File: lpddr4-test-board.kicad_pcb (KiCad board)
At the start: 8 copper layers, 117 x 86 mm, 266 parts, among them IC1 TPS54561, IC3 TPD8S009DSMR, J1 0878311420, J10 61300311121, J2 08B0-1X1T-36-F, J3 DC_SOCKET, J4 WE_629105150521, J5 2309409-1, J6 685119134923, J7 1140084168, Q2 BSS138APW, Q3 BSS138APW, Q4 BSS138APW, Q5 BSS138APW, Q6 BSS138APW, Q7 BSS138APW, Q8 BSS138APW, U1 XC7K70T-FBG484, U2 ASEM1-100.000MHZ-LC-T, U3 S25FL128SAGNFI000, U4 TPS65296, U5 TPS62823DLCT, U6 DP83848JSQ_NOPB, U7 FT4232HQ, Y1 ABM8G-25.000MHZ-18-D2Y-T

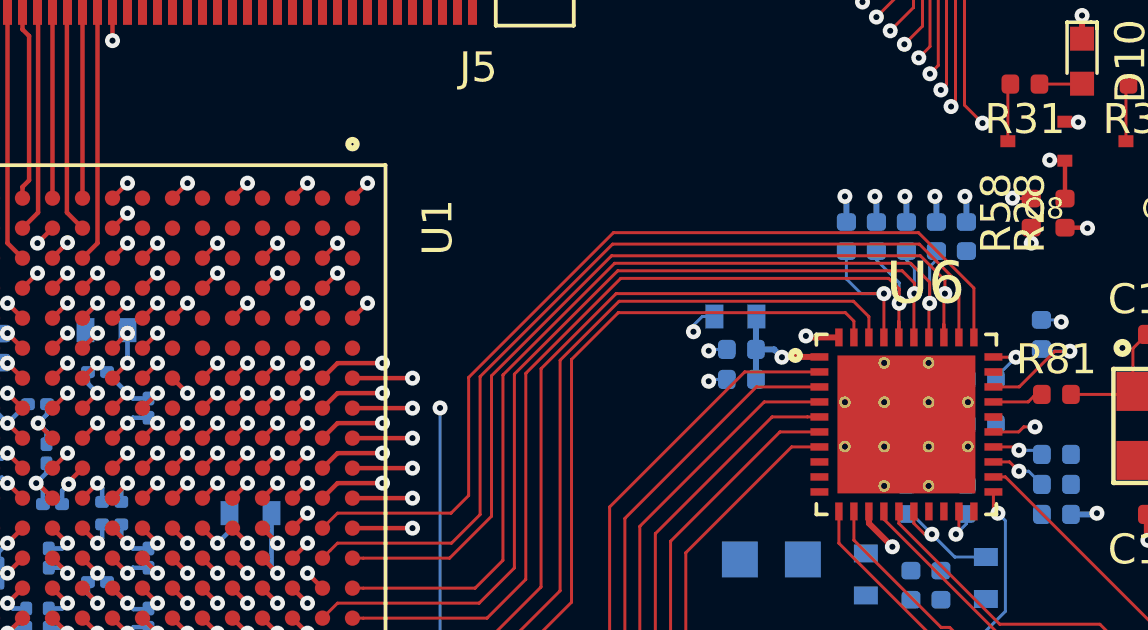
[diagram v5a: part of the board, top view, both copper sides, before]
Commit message: Change via assignment under FPGA
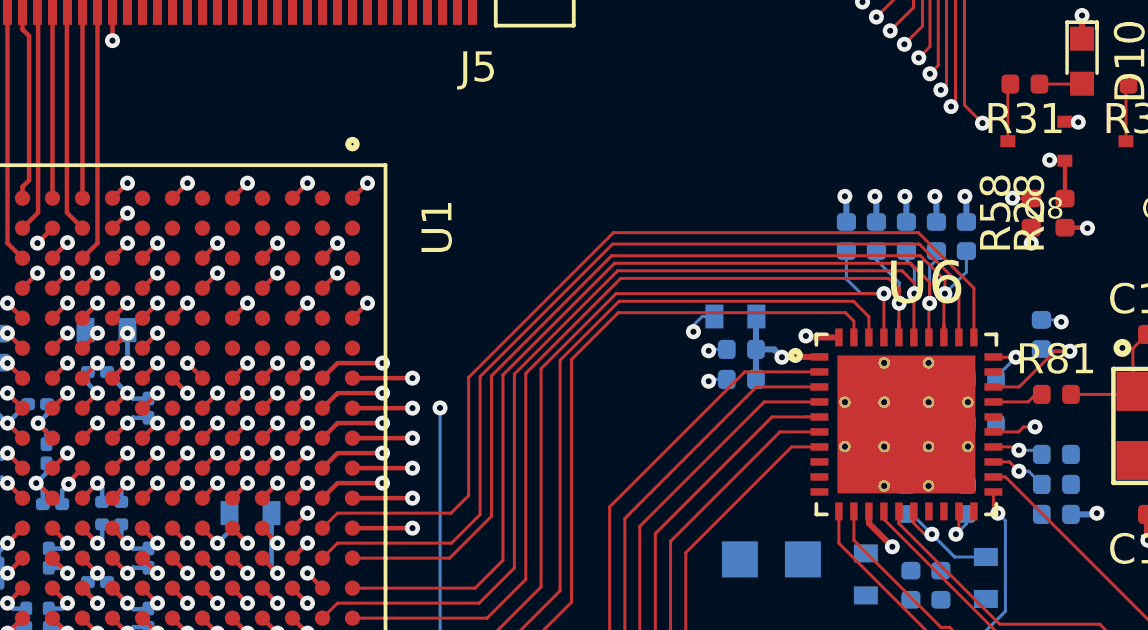
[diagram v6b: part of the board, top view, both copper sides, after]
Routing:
- net ETH_CRS: track 29.4 -> 31.1 mm
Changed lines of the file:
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@@
     (thickness 1.6)
     (drawings 130)
-    (tracks 3293)
+    (tracks 3297)
     (zones 0)
     (modules 266)
@@
   (segment (start 173.536329 89.497157) (end 174.036329 88.997157) (width 0.15) (layer F.Cu) (net 19))
   (via blind (at 174.036329 88.997157) (size 0.5) (drill 0.2) (layers F.Cu GND1) (net 19) (status 40000))
-  (segment (start 174.536329 91.497157) (end 175.036329 90.997156) (width 0.15) (layer F.Cu) (net 19))
-  (via blind (at 175.036329 90.997156) (size 0.5) (drill 0.2) (layers F.Cu GND1) (net 19) (status 40000))
+  (segment (start 174.536328 91.497156) (end 174.036327 90.997156) (width 0.15) (layer F.Cu) (net 19))
+  (via (at 174.036327 90.997156) (size 0.5) (drill 0.2) (layers F.Cu B.Cu) (net 19) (status 40000))
   (segment (start 175.536329 94.497156) (end 176.036328 93.997157) (width 0.15) (layer F.Cu) (net 19))
   (segment (start 175.536328 89.497157) (end 176.036328 88.997157) (width 0.15) (layer F.Cu) (net 19))
@@
   (segment (start 206.278 71.773) (end 204.506 71.773) (width 0.15) (layer F.Cu) (net 23))
   (segment (start 204.506 71.773) (end 204.49 71.789) (width 0.15) (layer F.Cu) (net 23))
-  (segment (start 204.49 75.726) (end 204.49 71.789) (width 0.1) (layer In2.Cu) (net 23))
-  (segment (start 196.1715 77.6945) (end 202.5215 77.6945) (width 0.1) (layer In2.Cu) (net 23))
-  (segment (start 171.370327 90.997156) (end 171.847171 91.474) (width 0.1) (layer In2.Cu) (net 23))
-  (segment (start 173.248 91.474) (end 174.264 90.458) (width 0.1) (layer In2.Cu) (net 23))
-  (segment (start 171.036329 90.997156) (end 171.370327 90.997156) (width 0.1) (layer In2.Cu) (net 23))
-  (segment (start 171.847171 91.474) (end 173.248 91.474) (width 0.1) (layer In2.Cu) (net 23))
-  (segment (start 174.264 90.458) (end 183.408 90.458) (width 0.1) (layer In2.Cu) (net 23))
-  (segment (start 202.5215 77.6945) (end 204.49 75.726) (width 0.1) (layer In2.Cu) (net 23))
-  (segment (start 183.408 90.458) (end 196.1715 77.6945) (width 0.1) (layer In2.Cu) (net 23))
   (segment (start 170.411328 90.997157) (end 171.036329 90.997156) (width 0.1) (layer In5.Cu) (net 23))
   (segment (start 168.620327 89.247157) (end 170.370327 90.997157) (width 0.1) (layer In5.Cu) (net 23))
@@
   (segment (start 153.161328 104.997157) (end 152.036328 106.122157) (width 0.1) (layer In5.Cu) (net 23))
   (segment (start 157.286328 89.247157) (end 157.536328 89.247157) (width 0.1) (layer In5.Cu) (net 23))
+  (segment (start 202.5215 77.6945) (end 204.49 75.726) (width 0.1) (layer In2.Cu) (net 23))
+  (segment (start 176.450485 90.458) (end 183.408 90.458) (width 0.1) (layer In2.Cu) (net 23))
+  (segment (start 175.434485 91.474) (end 176.450485 90.458) (width 0.1) (layer In2.Cu) (net 23))
+  (segment (start 196.1715 77.6945) (end 202.5215 77.6945) (width 0.1) (layer In2.Cu) (net 23))
+  (segment (start 171.370327 90.997156) (end 171.847171 91.474) (width 0.1) (layer In2.Cu) (net 23))
+  (segment (start 171.036329 90.997156) (end 171.370327 90.997156) (width 0.1) (layer In2.Cu) (net 23))
+  (segment (start 204.49 75.726) (end 204.49 71.789) (width 0.1) (layer In2.Cu) (net 23))
+  (segment (start 171.847171 91.474) (end 175.434485 91.474) (width 0.1) (layer In2.Cu) (net 23))
+  (segment (start 183.408 90.458) (end 196.1715 77.6945) (width 0.1) (layer In2.Cu) (net 23))
   (segment (start 169.536329 90.497157) (end 170.036329 89.997157) (width 0.15) (layer F.Cu) (net 24))
   (via blind (at 170.036329 89.997157) (size 0.5) (drill 0.2) (layers F.Cu In5.Cu) (net 24) (status 40000))
@@
   (segment (start 184.17 91.419136) (end 184.17 96.100866) (width 0.1) (layer F.Cu) (net 41))
   (segment (start 199.283 88.235502) (end 198.465478 87.41798) (width 0.1) (layer F.Cu) (net 41))
+  (segment (start 200 87.963) (end 199.283 88.68) (width 0.1) (layer B.Cu) (net 41))
+  (segment (start 200 87.263) (end 200 87.963) (width 0.1) (layer B.Cu) (net 41))
   (via (at 198.267 88.68) (size 0.5) (drill 0.2) (layers F.Cu B.Cu) (net 42))
   (segment (start 198.25 88.697) (end 198.267 88.68) (width 0.1) (layer F.Cu) (net 42))
@@
   (via blind (at 175.036329 91.997157) (size 0.5) (drill 0.2) (layers F.Cu In2.Cu) (net 90) (status 40000))
   (via (at 196.536328 78.95899) (size 0.5) (drill 0.2) (layers F.Cu B.Cu) (net 90))
-  (segment (start 196.109755 78.95899) (end 196.536328 78.95899) (width 0.1) (layer In2.Cu) (net 90))
-  (segment (start 184.181588 90.887157) (end 196.109755 78.95899) (width 0.1) (layer In2.Cu) (net 90))
-  (segment (start 176.146329 90.887157) (end 184.181588 90.887157) (width 0.1) (layer In2.Cu) (net 90))
-  (segment (start 175.036329 91.997157) (end 176.146329 90.887157) (width 0.1) (layer In2.Cu) (net 90))
   (segment (start 197.736328 77.75899) (end 196.536328 78.95899) (width 0.1) (layer F.Cu) (net 90))
   (segment (start 197.736328 73.397157) (end 197.736328 77.75899) (width 0.1) (layer F.Cu) (net 90))
@@
   (segment (start 190.036328 96.247157) (end 180.036328 96.247157) (width 0.1) (layer In2.Cu) (net 57))
   (segment (start 201.536328 93.122157) (end 201.286328 92.872157) (width 0.1) (layer In2.Cu) (net 57))
+  (segment (start 175.036329 91.997157) (end 175.389882 91.997157) (width 0.1) (layer In2.Cu) (net 90))
+  (segment (start 196.182775 78.95899) (end 196.536328 78.95899) (width 0.1) (layer In2.Cu) (net 90))
+  (segment (start 196.109755 78.95899) (end 196.182775 78.95899) (width 0.1) (layer In2.Cu) (net 90))
+  (segment (start 176.499882 90.887157) (end 184.181588 90.887157) (width 0.1) (layer In2.Cu) (net 90))
+  (segment (start 184.181588 90.887157) (end 196.109755 78.95899) (width 0.1) (layer In2.Cu) (net 90))
+  (segment (start 175.389882 91.997157) (end 176.499882 90.887157) (width 0.1) (layer In2.Cu) (net 90))
   (via (at 175.036329 99.997156) (size 0.5) (drill 0.2) (layers F.Cu B.Cu) (net 129) (status 40000))
   (segment (start 174.536329 99.497156) (end 175.036329 99.997156) (width 0.15) (layer F.Cu) (net 129))

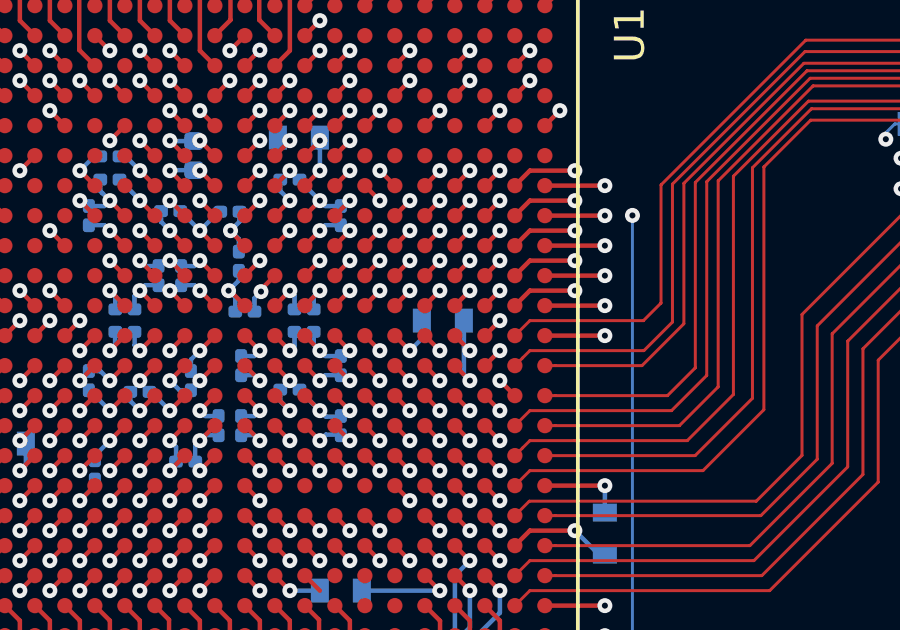
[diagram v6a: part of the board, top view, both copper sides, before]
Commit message: Change RGMII control signal assignment
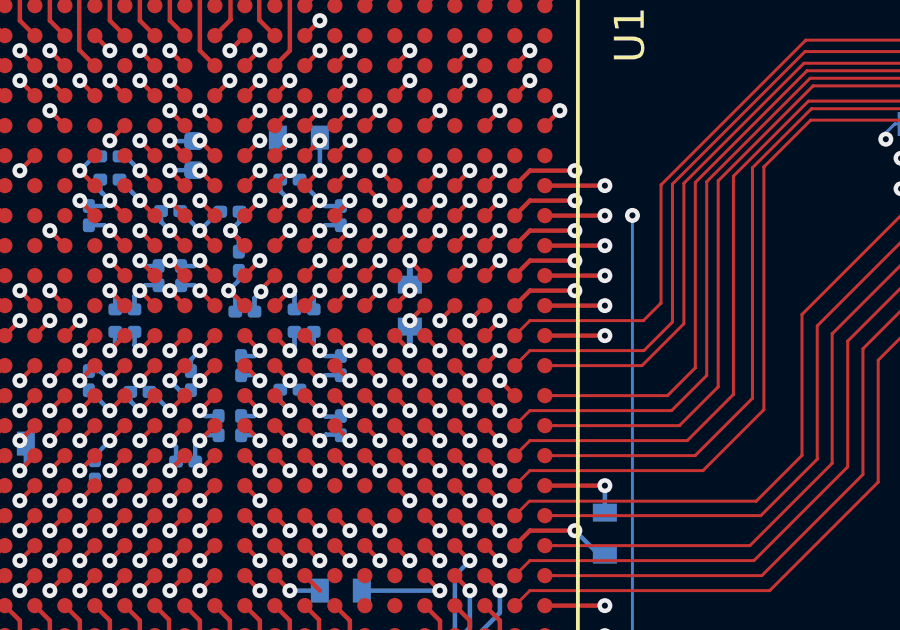
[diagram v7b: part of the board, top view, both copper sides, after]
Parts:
- moved C3 1.21 mm to (175.0, 95.5), turned to 90 degrees
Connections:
- U1 pad C12: ETH_MDIO -> ETH_REF_CLK
- U1 pad C13: ETH_TX_RSTN -> ETH_MDIO
- U1 pad C15: ETH_REF_CLK -> Net-(U1-PadC15)
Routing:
- net ETH_MDC: track 25.9 -> 31.0 mm
- net ETH_MDIO: track 26.5 -> 28.1 mm
- net ETH_TX_RSTN: track 1.46 -> 0.00 mm, vias 1 -> 0
- net GND: track 212.3 -> 211.3 mm
- net ETH_REF_CLK: track 28.4 -> 29.4 mm
- net Net-(U1-PadF10): track 0.71 -> 0.00 mm, vias 1 -> 0
- net Net-(U1-PadC15): track 0.00 -> 0.71 mm, vias 0 -> 1

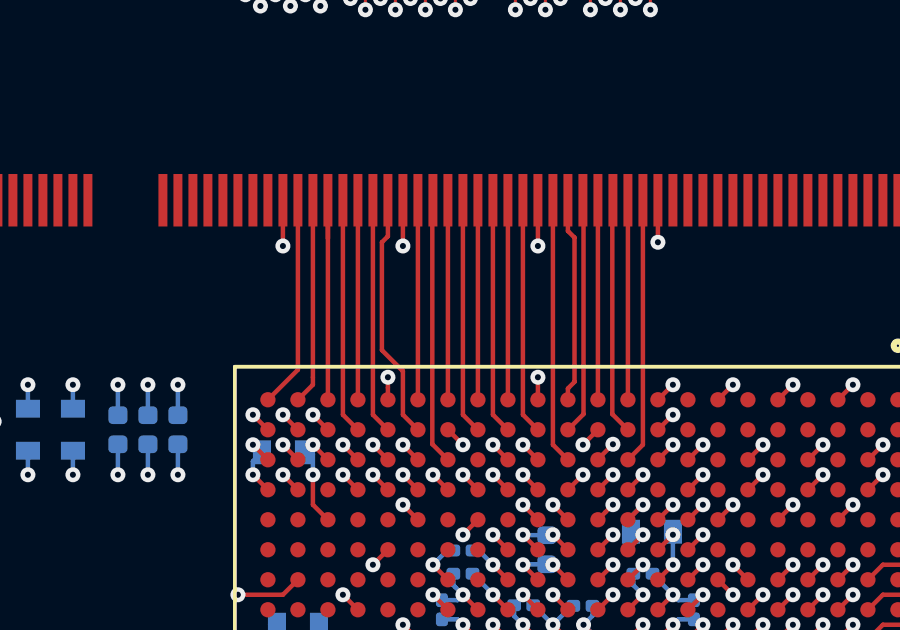
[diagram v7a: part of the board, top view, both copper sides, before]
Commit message: Update RGMII connector, started DRAM DQ equalization
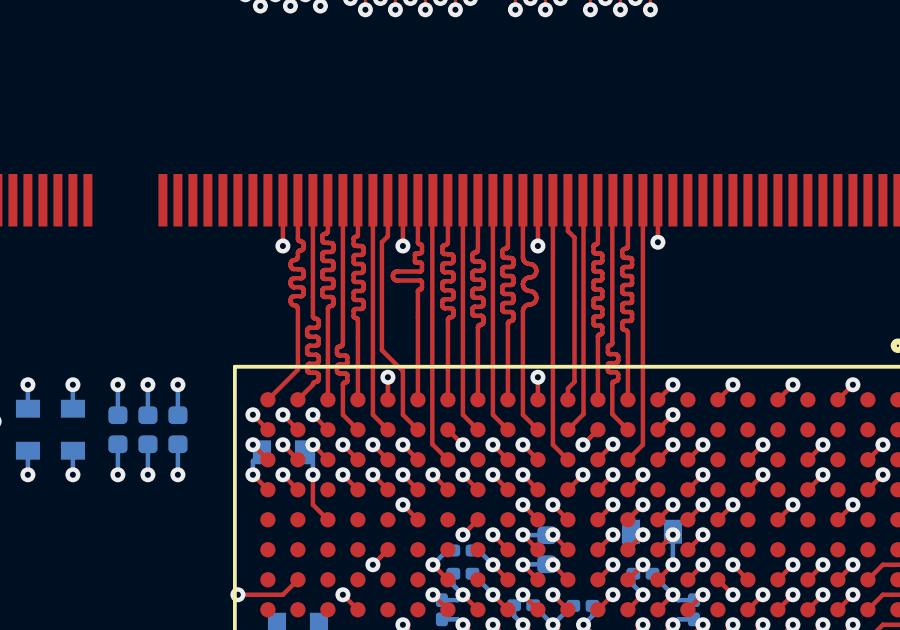
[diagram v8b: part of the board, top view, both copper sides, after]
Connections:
- U1 pad C15: Net-(U1-PadC15) -> ETH_RSTN
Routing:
- net ETH_RSTN: track 1.93 -> 30.7 mm, vias 1 -> 2
- net Net-(J5-Pad192): track 0.00 -> 19.2 mm, vias 0 -> 2
- net IO_N5: track 19.2 -> 0.00 mm, vias 2 -> 0
- net DMI_1A: track 6.62 -> 8.91 mm
- net DQ15_A: track 6.65 -> 8.93 mm
- net DQ04_A: track 6.65 -> 8.92 mm
- net DQ06_A: track 6.65 -> 8.92 mm
- net DQ13_A: track 6.65 -> 8.92 mm
- net DQ01_A: track 6.65 -> 8.92 mm
- net DQ03_A: track 6.65 -> 8.89 mm
- net DQ10_A: track 6.86 -> 8.90 mm
- net DQ11_A: track 7.06 -> 8.91 mm
- net DMI_0A: track 7.86 -> 8.88 mm
- net DQ08_A: track 7.86 -> 8.88 mm
- net DQ02_A: track 7.87 -> 8.88 mm
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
